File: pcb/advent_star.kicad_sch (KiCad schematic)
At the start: 20 parts, among them J1 TC2030, Q1 AO3401A, SW1 SW_Push_Dual, U1 CH32V003FxUx, U2 SC7A20

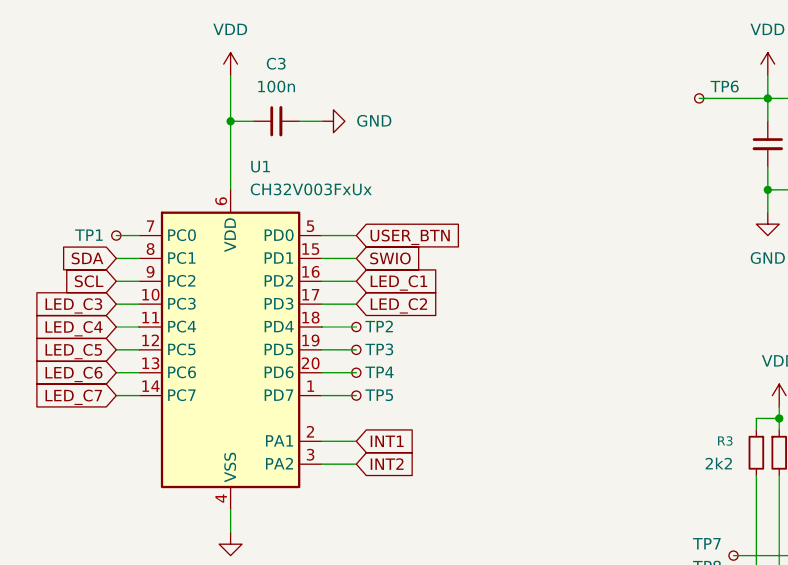
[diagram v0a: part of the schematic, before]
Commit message: changed pin mapping of I2C, all LED pins are now on a 'high current capable' pin
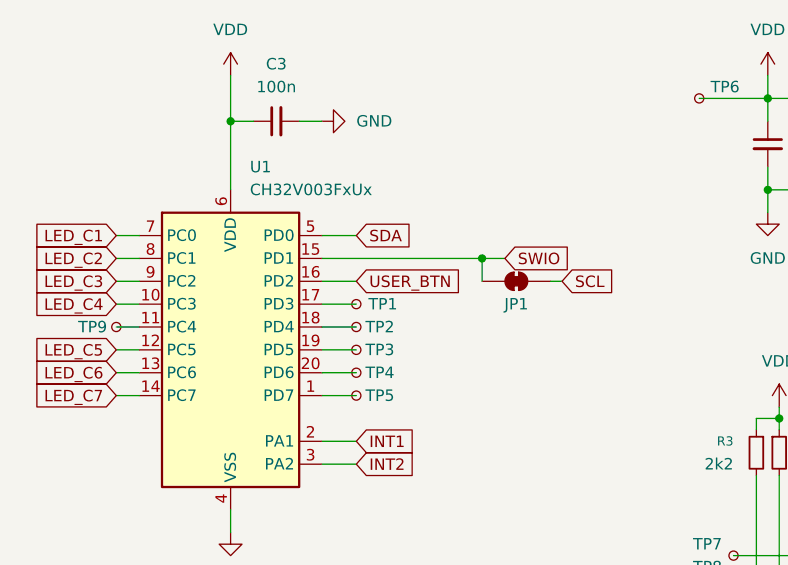
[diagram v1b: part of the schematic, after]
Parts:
- added JP1: SolderJumper_2_Bridged, Jumper:SolderJumper-2_P1.3mm_Bridged_RoundedPad1.0x1.5mm, symbol Jumper:SolderJumper_2_Bridged
- added TP9: TestPoint_Small, TestPoint:TestPoint_Pad_D1.0mm, symbol Connector:TestPoint_Small
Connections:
- net LED_C1: now also U1.7 (PC0); no longer U1.16 (PD2)
- net LED_C2: now also U1.8 (PC1); no longer U1.17 (PD3)
- net LED_C3: now also U1.9 (PC2); no longer U1.10 (PC3)
- net LED_C4: now also U1.10 (PC3); no longer U1.11 (PC4)
- net SCL: now also JP1.2 (B); no longer U1.9 (PC2)
- net SDA: now also U1.5 (PD0); no longer U1.8 (PC1)
- net SWIO: now also JP1.1 (A)
- net USER_BTN: now also U1.16 (PD2); no longer U1.5 (PD0)
- net at TP1.1: now also U1.17 (PD3); no longer U1.7 (PC0)
- new net: TP9.1, U1.11 (PC4)
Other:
- moved on the sheet: TP1

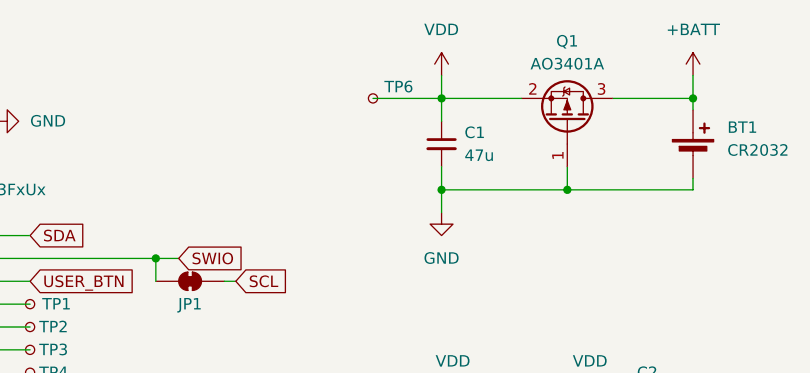
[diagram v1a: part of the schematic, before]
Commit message: charlieplex matrix finished, WIP on routing microcontroller
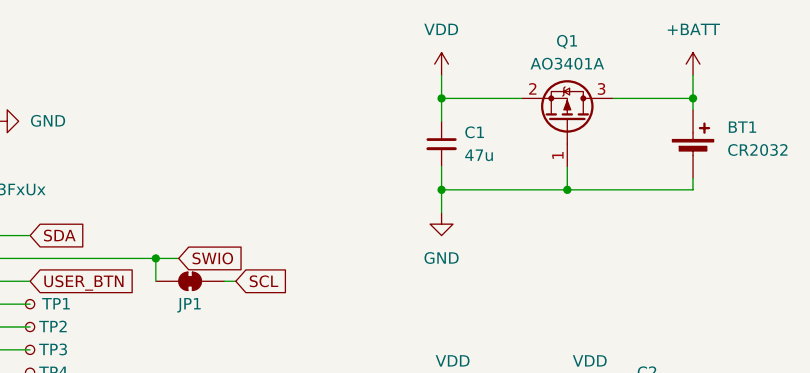
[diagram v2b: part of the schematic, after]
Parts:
- removed TP6: TestPoint_Small, TestPoint:TestPoint_Pad_D1.0mm, symbol Connector:TestPoint_Small
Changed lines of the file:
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@@
-	(wire
-		(pts
-			(xy 170.18 53.34) (xy 177.8 53.34)
-		)
-		(stroke
-			(width 0)
-			(type default)
-		)
-	)
 	(wire
 		(pts
@@
 					(unit 1)
 				)
-			)
-		)
-	)
-	(symbol
-		(lib_id "Connector:TestPoint_Small")
-		(at 170.18 53.34 0)
-		(unit 1)
-		(exclude_from_sim no)
-		(in_bom yes)
-		(on_board yes)
-		(dnp no)
-		(fields_autoplaced yes)
-		(property "Reference" "TP6"
-			(at 171.45 52.0699 0)
-			(effects
-				(font
-					(size 1.27 1.27)
-				)
-				(justify left)
-			)
-		)
-		(property "Value" "TestPoint_Small"
-			(at 171.45 54.6099 0)
-			(effects
-				(font
-					(size 1.27 1.27)
-				)
-				(justify left)
-				(hide yes)
-			)
-		)
-		(property "Footprint" "TestPoint:TestPoint_Pad_D1.0mm"
-			(at 175.26 53.34 0)
-			(effects
-				(font
-					(size 1.27 1.27)
-				)
-				(hide yes)
-			)
-		)
-		(property "Datasheet" "~"
-			(at 175.26 53.34 0)
-			(effects
-				(font
-					(size 1.27 1.27)
-				)
-				(hide yes)
-			)
-		)
-		(property "Description" "test point"
-			(at 170.18 53.34 0)
-			(effects
-				(font
-					(size 1.27 1.27)
-				)
-				(hide yes)
-			)
-		)
-		(pin "1"
-		)
-		(instances
-			(project "advent_star"
-				(path "/c94fd741-3317-4e4c-8137-e94188b66e79"
-					(reference "TP6")
-					(unit 1)
-				)

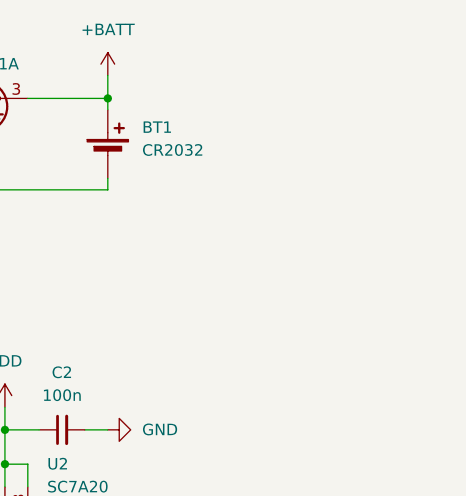
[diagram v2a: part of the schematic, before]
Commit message: almost done with routing, needs two ground pads to be connected
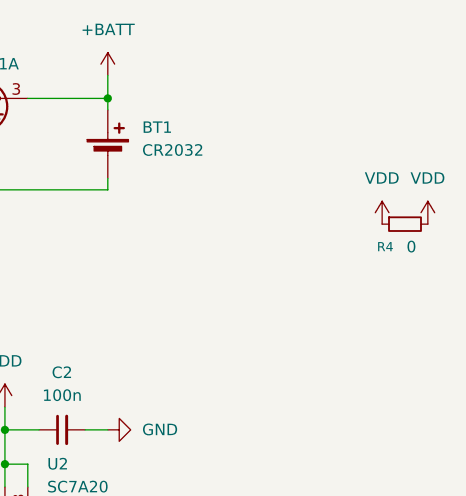
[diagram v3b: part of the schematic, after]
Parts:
- added R4: 0, Resistor_SMD:R_0603_1608Metric, symbol Device:R_Small
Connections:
- net VDD: now also R4.1, R4.2
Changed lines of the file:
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@@
+	(symbol
+		(lib_id "power:VDD")
+		(at 236.22 67.31 0)
+		(unit 1)
+		(exclude_from_sim no)
+		(in_bom yes)
+		(on_board yes)
+		(dnp no)
+		(fields_autoplaced yes)
+		(property "Reference" "#PWR016"
+			(at 236.22 71.12 0)
+			(effects
+				(font
+					(size 1.27 1.27)
+				)
+				(hide yes)
+			)
+		)
+		(property "Value" "VDD"
+			(at 236.22 62.23 0)
+			(effects
+				(font
+					(size 1.27 1.27)
+				)
+			)
+		)
+		(property "Footprint" ""
+			(at 236.22 67.31 0)
+			(effects
+				(font
+					(size 1.27 1.27)
+				)
+				(hide yes)
+			)
+		)
+		(property "Datasheet" ""
+			(at 236.22 67.31 0)
+			(effects
+				(font
+					(size 1.27 1.27)
+				)
+				(hide yes)
+			)
+		)
+		(property "Description" "Power symbol creates a global label with name \"VDD\""
+			(at 236.22 67.31 0)
+			(effects
+				(font
+					(size 1.27 1.27)
+				)
+				(hide yes)
+			)
+		)
+		(pin "1"
+		)
+		(instances
+			(project "advent_star"
+				(path "/c94fd741-3317-4e4c-8137-e94188b66e79"
+					(reference "#PWR016")
+					(unit 1)
+				)
+			)
+		)
+	)
 	(symbol
 		(lib_id "power:VDD")
@@
 				(path "/c94fd741-3317-4e4c-8137-e94188b66e79"
 					(reference "TP2")
+					(unit 1)
+				)
+			)
+		)
+	)
+	(symbol
+		(lib_id "power:VDD")
+		(at 241.3 67.31 0)
+		(unit 1)
+		(exclude_from_sim no)
+		(in_bom yes)
+		(on_board yes)
+		(dnp no)
+		(fields_autoplaced yes)
+		(property "Reference" "#PWR017"
+			(at 241.3 71.12 0)
+			(effects
+				(font
+					(size 1.27 1.27)
+				)
+				(hide yes)
+			)
+		)
+		(property "Value" "VDD"
+			(at 241.3 62.23 0)
+			(effects
+				(font
+					(size 1.27 1.27)
+				)
+			)
+		)
+		(property "Footprint" ""
+			(at 241.3 67.31 0)
+			(effects
+				(font
+					(size 1.27 1.27)
+				)
+				(hide yes)
+			)
+		)
+		(property "Datasheet" ""
+			(at 241.3 67.31 0)
+			(effects
+				(font
+					(size 1.27 1.27)
+				)
+				(hide yes)
+			)
+		)
+		(property "Description" "Power symbol creates a global label with name \"VDD\""
+			(at 241.3 67.31 0)
+			(effects
+				(font
+					(size 1.27 1.27)
+				)
+				(hide yes)
+			)
+		)
+		(pin "1"
+		)
+		(instances
+			(project "advent_star"
+				(path "/c94fd741-3317-4e4c-8137-e94188b66e79"
+					(reference "#PWR017")
 					(unit 1)
 				)
@@
 					(unit 1)
 				)
+			)
+		)
+	)
+	(symbol
+		(lib_id "Device:R_Small")
+		(at 238.76 67.31 90)
+		(mirror x)
+		(unit 1)
+		(exclude_from_sim no)
+		(in_bom yes)
+		(on_board yes)
+		(dnp no)
+		(property "Reference" "R4"
+			(at 237.4899 69.85 90)
+			(effects
+				(font
+					(size 1.016 1.016)
+				)
+				(justify left)
+			)
+		)
+		(property "Value" "0"
+			(at 240.0299 69.85 90)
+			(effects
+				(font
+					(size 1.27 1.27)
+				)
+				(justify left)
+			)
+		)
+		(property "Footprint" "Resistor_SMD:R_0603_1608Metric"
+			(at 238.76 67.31 0)
+			(effects
+				(font
+					(size 1.27 1.27)
+				)
+				(hide yes)
+			)
+		)
+		(property "Datasheet" "~"
+			(at 238.76 67.31 0)
+			(effects
+				(font
+					(size 1.27 1.27)
+				)
+				(hide yes)
+			)
+		)
+		(property "Description" "Resistor, small symbol"
+			(at 238.76 67.31 0)
+			(effects
+				(font
+					(size 1.27 1.27)
+				)
+				(hide yes)
+			)
+		)
+		(pin "1"
+		)
+		(pin "2"
+		)
+		(instances
+			(project "advent_star"
+				(path "/c94fd741-3317-4e4c-8137-e94188b66e79"
+					(reference "R4")
+					(unit 1)
+				)
